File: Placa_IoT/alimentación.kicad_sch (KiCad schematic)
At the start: 0 parts

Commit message: Alimentación creada
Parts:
- added C1, C2, C3, C4: 100 nf, Capacitor_SMD:C_0402_1005Metric, symbol Device:C
- added R1, R2: 10 kOhm, Resistor_SMD:R_0402_1005Metric, symbol Device:R
- added U1, U2: RT9080-33GJ5, ic_power:TSOT-23-5_RIT, symbol IC_power:RT9080-33GJ5
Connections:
- new net: R1.2, U1.3 (EN)
- new net: R2.2, U2.3 (EN)
- new net +3.3V: C2.1, U1.5 (VOUT)
- new net +3.3VP: C4.1, U2.5 (VOUT)
- new net +5V: C1.1, C3.1, R1.1, R2.1, U1.1 (VIN), U2.1 (VIN)
- new net GND: C1.2, C2.2, C3.2, C4.2, U1.2 (GND), U2.2 (GND)

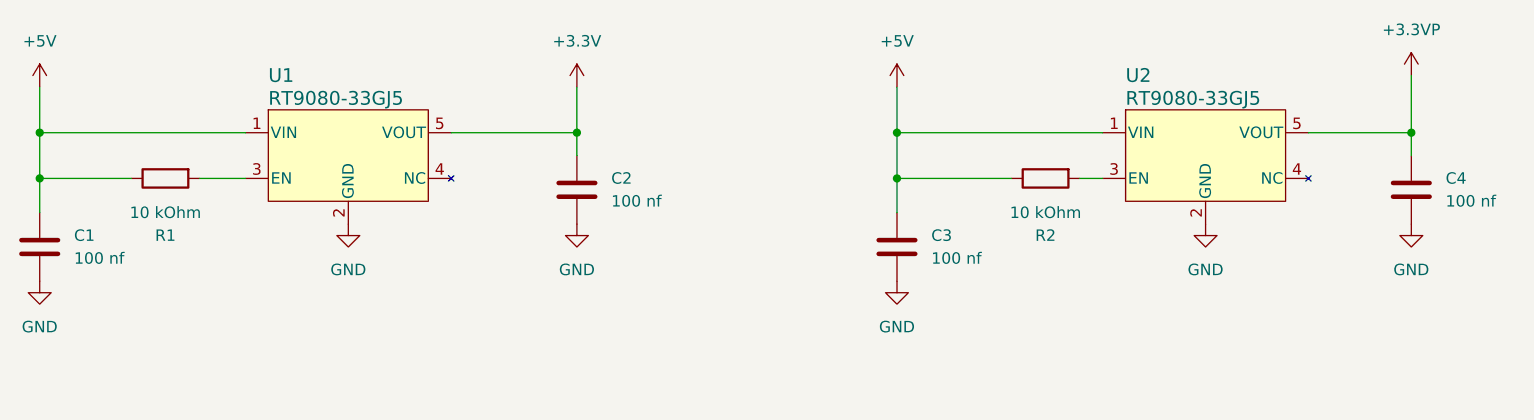
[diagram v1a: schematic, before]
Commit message: Añadida Etiqueta resistencia NC
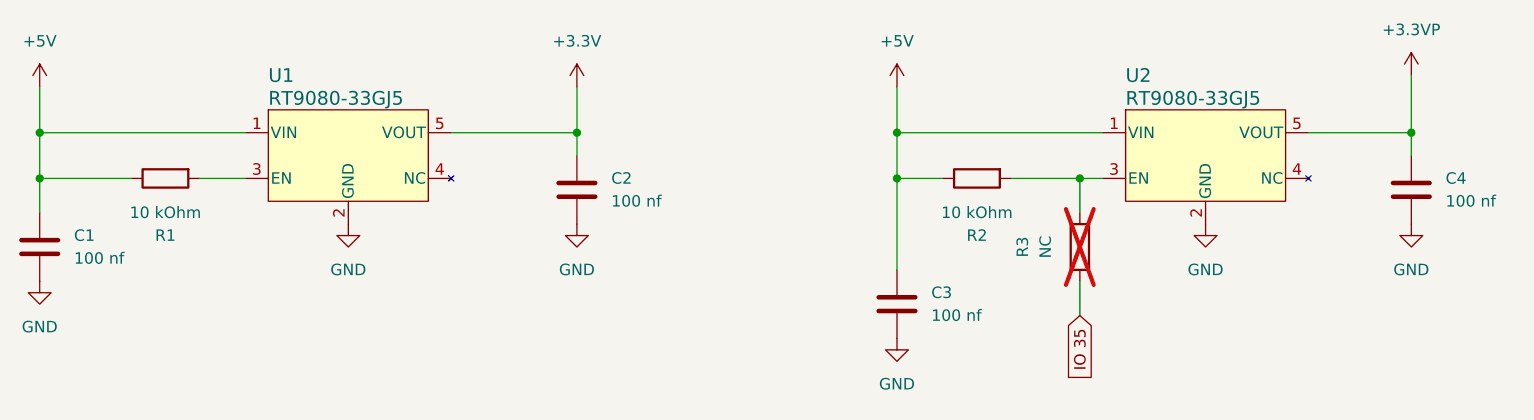
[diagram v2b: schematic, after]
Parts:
- added R3: NC, Resistor_SMD:R_0402_1005Metric, symbol Device:R
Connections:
- net at R2.2, U2.3 (EN): now also R3.2
- new net IO 35: R3.1
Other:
- moved on the sheet: C3, R2
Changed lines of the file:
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@@
+	)
+	(junction
+		(at 190.5 71.12)
+		(diameter 0)
+		(color 0 0 0 0)
 	)
 	(junction
@@
 	(wire
 		(pts
+			(xy 190.5 82.55) (xy 190.5 86.36)
+		)
+		(stroke
+			(width 0)
+			(type default)
+		)
+	)
+	(wire
+		(pts
 			(xy 74.93 66.04) (xy 74.93 71.12)
 		)
@@
 	(wire
 		(pts
-			(xy 170.18 71.12) (xy 182.88 71.12)
-		)
-		(stroke
-			(width 0)
-			(type default)
-		)
-	)
-	(wire
-		(pts
-			(xy 170.18 71.12) (xy 170.18 74.93)
+			(xy 170.18 71.12) (xy 175.26 71.12)
+		)
+		(stroke
+			(width 0)
+			(type default)
+		)
+	)
+	(wire
+		(pts
+			(xy 170.18 71.12) (xy 170.18 81.28)
 		)
 		(stroke
@@
 	(wire
 		(pts
+			(xy 182.88 71.12) (xy 190.5 71.12)
+		)
+		(stroke
+			(width 0)
+			(type default)
+		)
+	)
+	(wire
+		(pts
+			(xy 190.5 71.12) (xy 190.5 74.93)
+		)
+		(stroke
+			(width 0)
+			(type default)
+		)
+	)
+	(wire
+		(pts
+			(xy 170.18 66.04) (xy 193.04 66.04)
+		)
+		(stroke
+			(width 0)
+			(type default)
+		)
+	)
+	(wire
+		(pts
+			(xy 120.65 66.04) (xy 134.62 66.04)
+		)
+		(stroke
+			(width 0)
+			(type default)
+		)
+	)
+	(wire
+		(pts
+			(xy 170.18 66.04) (xy 170.18 71.12)
+		)
+		(stroke
+			(width 0)
+			(type default)
+		)
+	)
+	(wire
+		(pts
+			(xy 134.62 68.58) (xy 134.62 66.04)
+		)
+		(stroke
+			(width 0)
+			(type default)
+		)
+	)
+	(wire
+		(pts
+			(xy 227.33 59.69) (xy 227.33 66.04)
+		)
+		(stroke
+			(width 0)
+			(type default)
+		)
+	)
+	(wire
+		(pts
 			(xy 190.5 71.12) (xy 193.04 71.12)
 		)
@@
 		)
 	)
-	(wire
-		(pts
-			(xy 170.18 66.04) (xy 193.04 66.04)
-		)
-		(stroke
-			(width 0)
-			(type default)
-		)
-	)
-	(wire
-		(pts
-			(xy 120.65 66.04) (xy 134.62 66.04)
-		)
-		(stroke
-			(width 0)
-			(type default)
-		)
-	)
-	(wire
-		(pts
-			(xy 170.18 66.04) (xy 170.18 71.12)
-		)
-		(stroke
-			(width 0)
-			(type default)
-		)
-	)
-	(wire
-		(pts
-			(xy 134.62 68.58) (xy 134.62 66.04)
-		)
-		(stroke
-			(width 0)
-			(type default)
-		)
-	)
-	(wire
-		(pts
-			(xy 227.33 59.69) (xy 227.33 66.04)
-		)
-		(stroke
-			(width 0)
-			(type default)
+	(global_label "IO 35"
+		(shape input)
+		(at 190.5 86.36 270)
+		(fields_autoplaced yes)
+		(effects
+			(font
+				(size 1.27 1.27)
+			)
+			(justify right)
+		)
+		(property "Intersheetrefs" "${INTERSHEET_REFS}"
+			(at 190.5 94.6671 90)
+			(hide yes)
+			(show_name no)
+			(do_not_autoplace no)
+			(effects
+				(font
+					(size 1.27 1.27)
+				)
+				(justify right)
+			)
 		)
 	)
@@
 	(symbol
 		(lib_id "Device:R")
-		(at 186.69 71.12 90)
+		(at 179.07 71.12 90)
 		(mirror x)
 		(unit 1)
@@
 		(dnp no)
 		(property "Reference" "R2"
-			(at 186.69 77.47 90)
+			(at 179.07 77.47 90)
 			(show_name no)
 			(do_not_autoplace no)
@@
 		)
 		(property "Value" "10 kOhm"
-			(at 186.69 74.93 90)
+			(at 179.07 74.93 90)
 			(show_name no)
 			(do_not_autoplace no)
@@
 		)
 		(property "Footprint" "Resistor_SMD:R_0402_1005Metric"
-			(at 186.69 69.342 90)
+			(at 179.07 69.342 90)
 			(hide yes)
 			(show_name no)
@@
 		)
 		(property "Datasheet" ""
-			(at 186.69 71.12 0)
+			(at 179.07 71.12 0)
 			(hide yes)
 			(show_name no)
@@
 		)
 		(property "Description" "Resistor"
-			(at 186.69 71.12 0)
+			(at 179.07 71.12 0)
 			(hide yes)
 			(show_name no)
@@
 	(symbol
 		(lib_id "power:GND")
-		(at 170.18 82.55 0)
+		(at 170.18 88.9 0)
 		(unit 1)
 		(body_style 1)
@@
 		(fields_autoplaced yes)
 		(property "Reference" "#PWR09"
+			(at 170.18 95.25 0)
+			(hide yes)
+			(show_name no)
+			(do_not_autoplace no)
+			(effects
+				(font
+					(size 1.27 1.27)
+				)
+			)
+		)
+		(property "Value" "GND"
+			(at 170.18 93.98 0)
+			(show_name no)
+			(do_not_autoplace no)
+			(effects
+				(font
+					(size 1.27 1.27)
+				)
+			)
+		)
+		(property "Footprint" ""
 			(at 170.18 88.9 0)
 			(hide yes)
@@
 			)
 		)
-		(property "Value" "GND"
-			(at 170.18 87.63 0)
-			(show_name no)
-			(do_not_autoplace no)
-			(effects
-				(font
-					(size 1.27 1.27)
-				)
-			)
-		)
-		(property "Footprint" ""
-			(at 170.18 82.55 0)
-			(hide yes)
-			(show_name no)
-			(do_not_autoplace no)
-			(effects
-				(font
-					(size 1.27 1.27)
-				)
-			)
-		)
 		(property "Datasheet" ""
-			(at 170.18 82.55 0)
+			(at 170.18 88.9 0)
 			(hide yes)
 			(show_name no)
@@
 		)
 		(property "Description" "Power symbol creates a global label with name \"GND\" , ground"
-			(at 170.18 82.55 0)
+			(at 170.18 88.9 0)
 			(hide yes)
 			(show_name no)
@@
 	(symbol
 		(lib_id "Device:C")
-		(at 170.18 78.74 0)
+		(at 170.18 85.09 0)
 		(unit 1)
 		(body_style 1)
@@
 		(fields_autoplaced yes)
 		(property "Reference" "C3"
-			(at 173.99 77.4699 0)
+			(at 173.99 83.8199 0)
 			(show_name no)
 			(do_not_autoplace no)
@@
 		)
 		(property "Value" "100 nf"
-			(at 173.99 80.0099 0)
+			(at 173.99 86.3599 0)
 			(show_name no)
 			(do_not_autoplace no)
@@
 		)
 		(property "Footprint" "Capacitor_SMD:C_0402_1005Metric"
-			(at 171.1452 82.55 0)
+			(at 171.1452 88.9 0)
 			(hide yes)
 			(show_name no)
@@
 		)
 		(property "Datasheet" ""
-			(at 170.18 78.74 0)
+			(at 170.18 85.09 0)
 			(hide yes)
 			(show_name no)
@@
 		)
 		(property "Description" "Unpolarized capacitor"
-			(at 170.18 78.74 0)
+			(at 170.18 85.09 0)
 			(hide yes)
 			(show_name no)
@@
 					(unit 1)
 				)
+			)
+		)
+	)
+	(symbol
+		(lib_id "Device:R")
+		(at 190.5 78.74 180)
+		(unit 1)
+		(body_style 1)
+		(exclude_from_sim no)
+		(in_bom yes)
+		(on_board yes)
+		(in_pos_files yes)
+		(dnp yes)
+		(property "Reference" "R3"
+			(at 184.15 78.74 90)
+			(show_name no)
+			(do_not_autoplace no)
+			(effects
+				(font
+					(size 1.27 1.27)
+				)
+			)
+		)
+		(property "Value" "NC"
+			(at 186.69 78.74 90)
+			(show_name no)
+			(do_not_autoplace no)
+			(effects
+				(font
+					(size 1.27 1.27)
+				)
+			)
+		)
+		(property "Footprint" "Resistor_SMD:R_0402_1005Metric"
+			(at 192.278 78.74 90)
+			(hide yes)
+			(show_name no)
+			(do_not_autoplace no)
+			(effects
+				(font
+					(size 1.27 1.27)
+				)
+			)
+		)
+		(property "Datasheet" ""
+			(at 190.5 78.74 0)
+			(hide yes)
+			(show_name no)
+			(do_not_autoplace no)
+			(effects
+				(font
+					(size 1.27 1.27)
+				)
+			)
+		)
+		(property "Description" "Resistor"
+			(at 190.5 78.74 0)
+			(hide yes)
+			(show_name no)
+			(do_not_autoplace no)
+			(effects
+				(font
+					(size 1.27 1.27)
+				)
+			)
+		)
+		(pin "1"
+		)
+		(pin "2"
+		)
+		(instances
+			(project "Placa_IoT"
+				(path "/c2afb48e-650f-42bf-8711-71f0f8e70388/3d73536a-b6dd-4ab5-8664-cf2616aa5b65"
+					(reference "R3")
+					(unit 1)
+				)
